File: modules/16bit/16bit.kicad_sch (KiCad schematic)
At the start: 56 parts, among them J1 Conn_01x08_Socket, J2 Conn_01x08_Socket, J5 USB_C_Receptacle_USB2.0_14P, SW1 K2-1808SN-A4SW-01, SW2 K2-1808SN-A4SW-01, SW3 K2-1808SN-A4SW-01, U1 RP2350_60QFN, U2 W25Q128JVS, U3 MCP6002-xSN, U4 PT8211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

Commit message: set 1k for the DAC low pass filter
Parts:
- R17, R18: value 10k -> 1k
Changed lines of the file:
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@@
 			)
 		)
-		(property "Value" "10k"
+		(property "Value" "1k"
 			(at 194.31 276.8599 0)
 			(effects
@@
 			)
 		)
-		(property "Value" "10k"
+		(property "Value" "1k"
 			(at 180.34 276.8599 0)
 			(effects

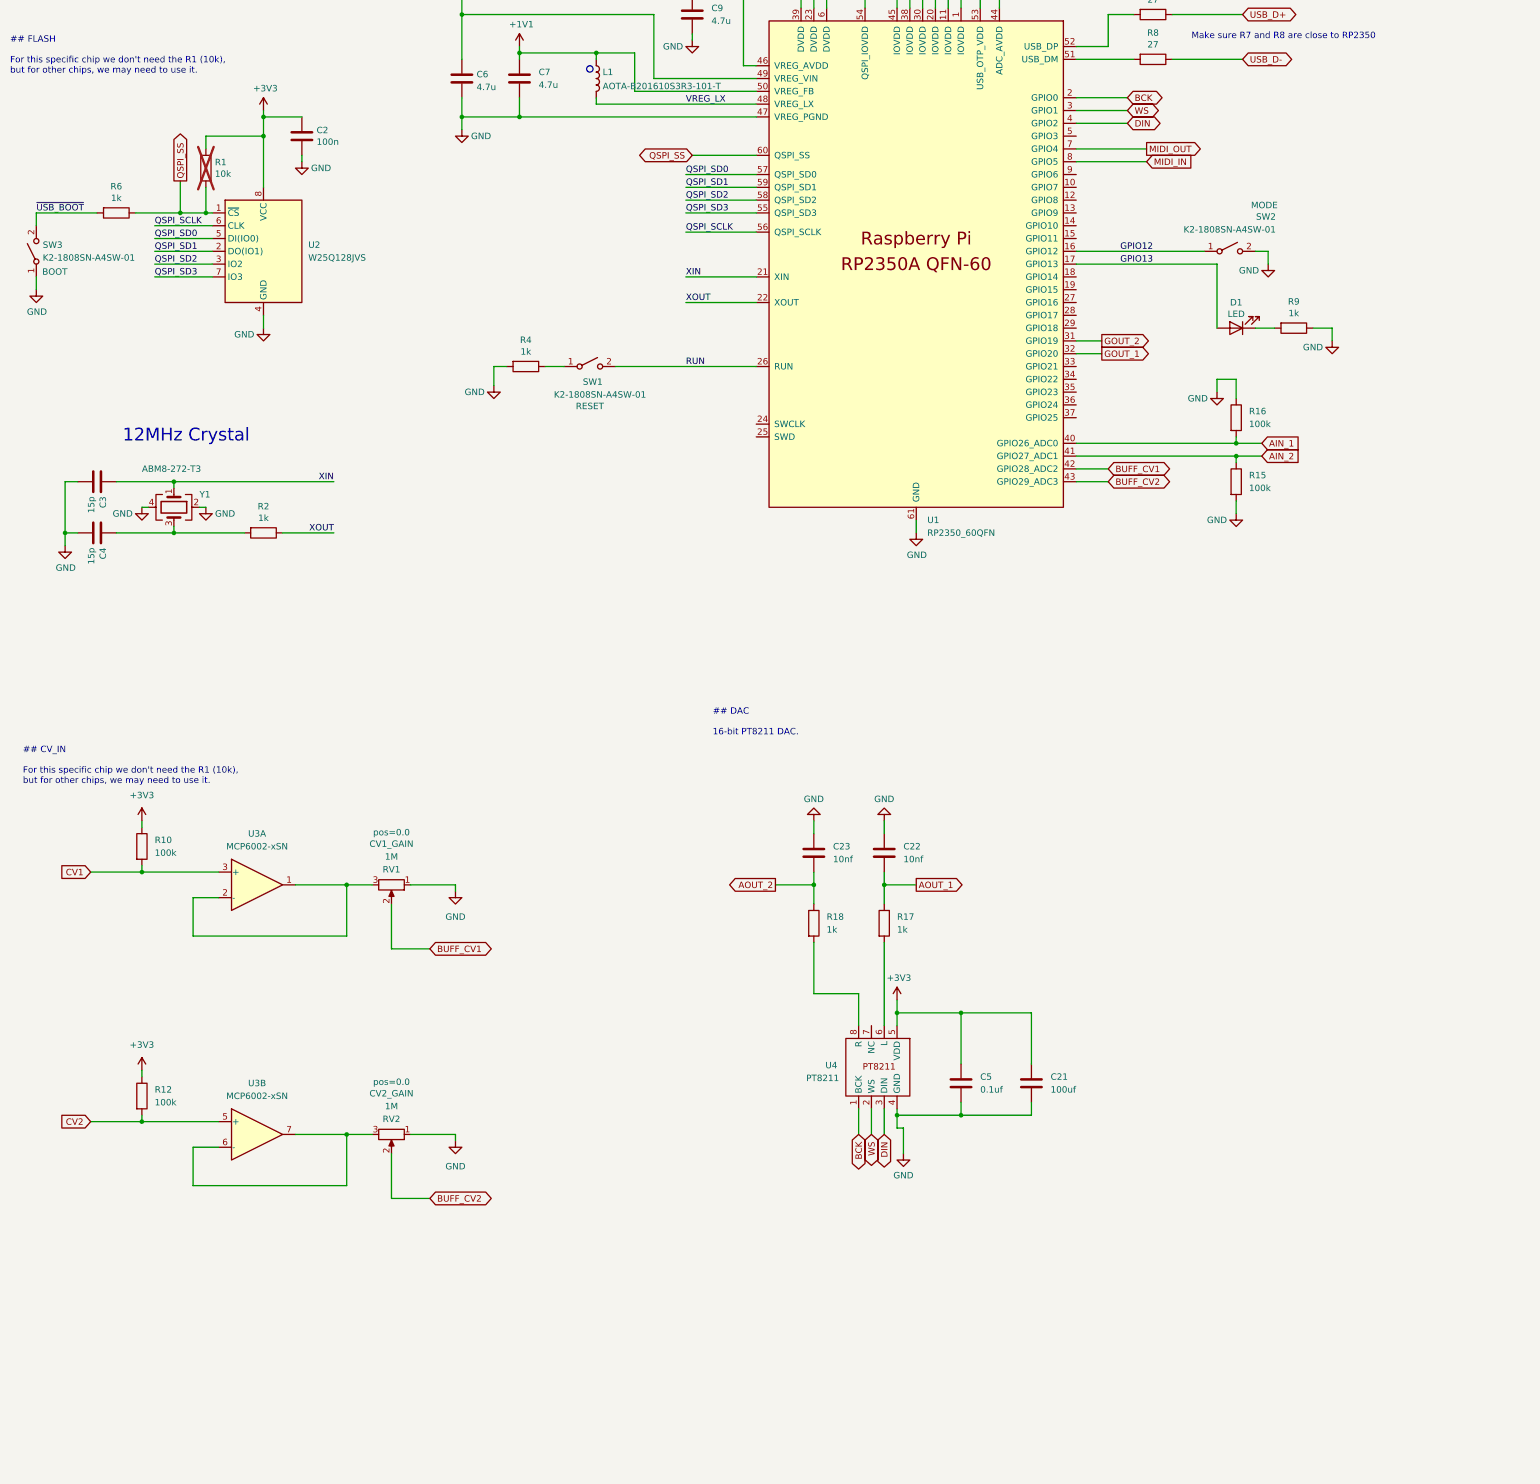
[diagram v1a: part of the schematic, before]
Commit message: Add 4677 PSRAM
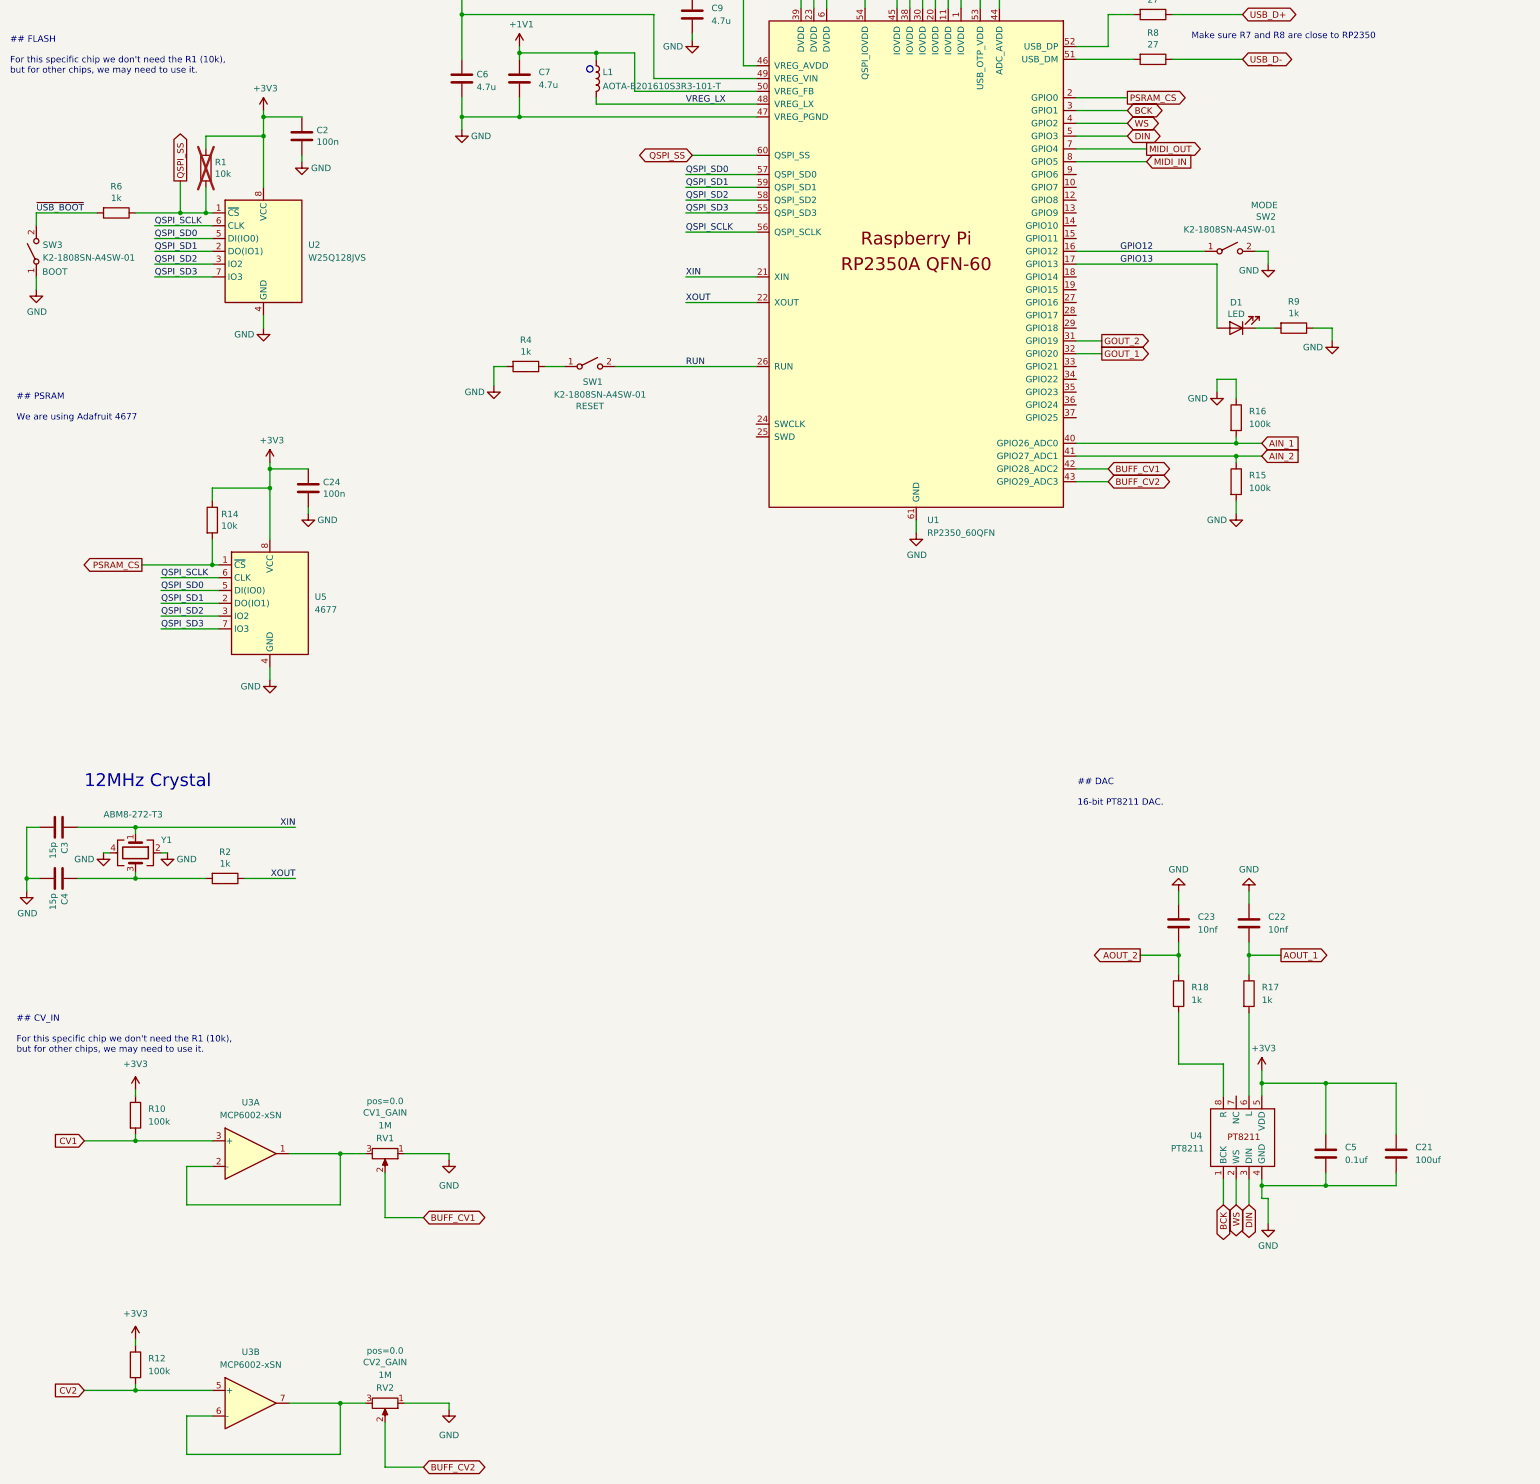
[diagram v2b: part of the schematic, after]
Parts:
- added C24: 100n, Capacitor_SMD:C_0402_1005Metric, symbol Device:C
- added R14: 10k, Resistor_SMD:R_0402_1005Metric, symbol Device:R
- added U5: 4677, BreadModular_MISC:SOIC-8 Generic, symbol Memory_Flash:W25Q128JVS
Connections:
- net +3V3: now also C24.1, R14.1, U5.8 (VCC)
- net BCK: now also U1.3 (GPIO1); no longer U1.2 (GPIO0)
- net DIN: now also U1.5 (GPIO3); no longer U1.4 (GPIO2)
- net GND: now also C24.2, U5.4 (GND)
- net QSPI_SCLK: now also U5.6 (CLK)
- net QSPI_SD0: now also U5.5 (DI(IO0))
- net QSPI_SD1: now also U5.2 (DO(IO1))
- net QSPI_SD2: now also U5.3 (IO2)
- net QSPI_SD3: now also U5.7 (IO3)
- net WS: now also U1.4 (GPIO2); no longer U1.3 (GPIO1)
- new net PSRAM_CS: R14.2, U1.2 (GPIO0), U5.1 (~{CS})
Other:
- note added: "## PSRAM We are using Adafruit 4677"
- moved on the sheet: C21, C22, C23, C3, C4, C5, R10, R12, R17, R18, R2, RV1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

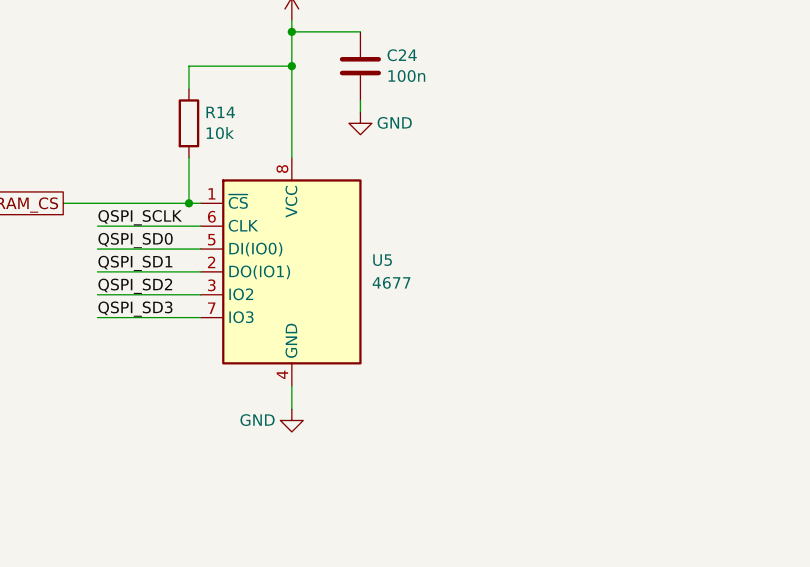
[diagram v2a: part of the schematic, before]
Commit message: 16bit: update PSRAM support
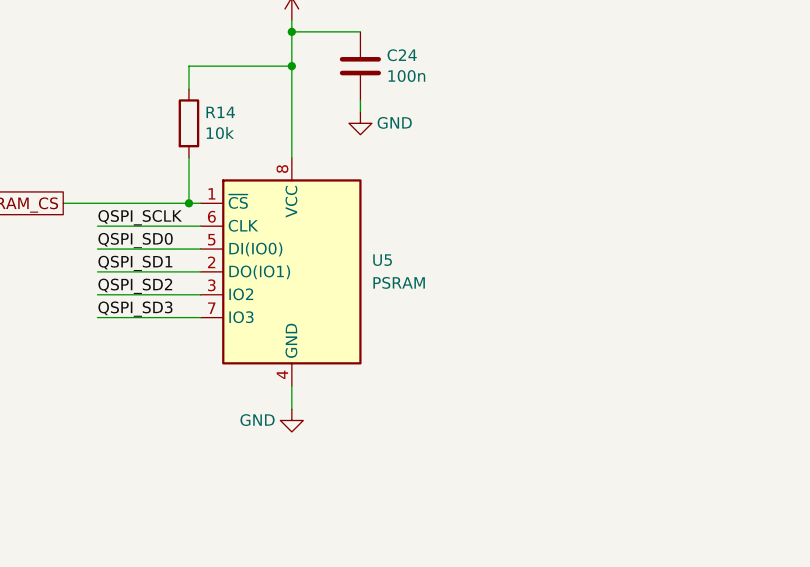
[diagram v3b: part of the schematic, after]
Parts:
- U5: value 4677 -> PSRAM
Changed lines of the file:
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@@
 			)
 		)
-		(property "Value" "4677"
+		(property "Value" "PSRAM"
 			(at 78.74 213.3599 0)
 			(effects

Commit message: 16bit: Add Ditial Audio In & Out support As of now this is currently hardware only. But this allows us to send audio out and in between 16bits digital using a single pin
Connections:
- net DGITIAL_AUDIO_IN: now reaches U1.12 (GPIO8)
- net DGITIAL_AUDIO_IN: now also J1.5 (Pin_5)
- net CV2: no longer names the net of R12.2, U3.5 (+)
- net CV2: no longer J1.5 (Pin_5)
- net GOUT_2 renamed DGITIAL_AUDIO_OUT
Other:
- moved on the sheet: J2
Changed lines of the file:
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@@
 	)
 	(junction
-		(at 43.18 368.3)
-		(diameter 0)
-		(color 0 0 0 0)
-	)
-	(junction
 		(at 214.63 81.28)
 		(diameter 0)
@@
 	(wire
 		(pts
+			(xy 240.03 132.08) (xy 229.87 132.08)
+		)
+		(stroke
+			(width 0)
+			(type default)
+		)
+	)
+	(wire
+		(pts
 			(xy 105.41 322.58) (xy 105.41 321.31)
 		)
@@
 	(wire
 		(pts
-			(xy 463.55 128.27) (xy 469.9 128.27)
+			(xy 83.82 370.84) (xy 83.82 381)
 		)
 		(stroke
@@
 	(wire
 		(pts
-			(xy 83.82 370.84) (xy 83.82 381)
+			(xy 229.87 114.3) (xy 240.03 114.3)
 		)
 		(stroke
@@
 	(wire
 		(pts
-			(xy 229.87 114.3) (xy 240.03 114.3)
+			(xy 266.7 307.34) (xy 279.4 307.34)
 		)
 		(stroke
@@
 	(wire
 		(pts
-			(xy 266.7 307.34) (xy 279.4 307.34)
+			(xy 21.59 266.7) (xy 21.59 269.24)
 		)
 		(stroke
@@
 	(wire
 		(pts
-			(xy 21.59 266.7) (xy 21.59 269.24)
+			(xy 537.21 71.12) (xy 539.75 71.12)
 		)
 		(stroke
@@
 	(wire
 		(pts
-			(xy 537.21 71.12) (xy 539.75 71.12)
+			(xy 40.64 69.85) (xy 40.64 80.01)
 		)
 		(stroke
@@
 	(wire
 		(pts
-			(xy 40.64 69.85) (xy 40.64 80.01)
+			(xy 199.39 93.98) (xy 199.39 81.28)
 		)
 		(stroke
@@
 	(wire
 		(pts
-			(xy 199.39 93.98) (xy 199.39 81.28)
+			(xy 469.9 128.27) (xy 463.55 128.27)
 		)
 		(stroke
@@
 	(wire
 		(pts
-			(xy 502.92 125.73) (xy 508 125.73)
-		)
-		(stroke
-			(width 0)
-			(type default)
-		)
-	)
-	(wire
-		(pts
 			(xy 201.93 93.98) (xy 201.93 81.28)
 		)
@@
 	(wire
 		(pts
-			(xy 502.92 120.65) (xy 508 120.65)
+			(xy 525.78 121.92) (xy 530.86 121.92)
 		)
 		(stroke
@@
 	(wire
 		(pts
-			(xy 33.02 368.3) (xy 43.18 368.3)
-		)
-		(stroke
-			(width 0)
-			(type default)
-		)
-	)
-	(wire
-		(pts
 			(xy 143.51 60.96) (xy 154.94 60.96)
 		)
@@
 	(wire
 		(pts
-			(xy 502.92 118.11) (xy 508 118.11)
+			(xy 525.78 119.38) (xy 530.86 119.38)
 		)
 		(stroke
@@
 	(wire
 		(pts
+			(xy 525.78 127) (xy 530.86 127)
+		)
+		(stroke
+			(width 0)
+			(type default)
+		)
+	)
+	(wire
+		(pts
 			(xy 537.21 212.09) (xy 529.59 212.09)
 		)
@@
 	(wire
 		(pts
-			(xy 502.92 115.57) (xy 508 115.57)
+			(xy 525.78 116.84) (xy 530.86 116.84)
 		)
 		(stroke
@@
 	(wire
 		(pts
-			(xy 502.92 123.19) (xy 508 123.19)
+			(xy 525.78 124.46) (xy 530.86 124.46)
 		)
 		(stroke
@@
 		)
 	)
-	(global_label "CV2"
-		(shape input)
-		(at 469.9 128.27 0)
-		(fields_autoplaced yes)
-		(effects
-			(font
-				(size 1.27 1.27)
-			)
-			(justify left)
-		)
-		(property "Intersheetrefs" "${INTERSHEET_REFS}"
-			(at 475.7991 128.27 0)
-			(effects
-				(font
-					(size 1.27 1.27)
-				)
-				(justify left)
-				(hide yes)
-			)
-		)
-	)
 	(global_label "GOUT_1"
 		(shape output)
@@
 	(global_label "GOUT_1"
 		(shape output)
-		(at 502.92 123.19 180)
+		(at 525.78 124.46 180)
 		(fields_autoplaced yes)
 		(effects
@@
 		)
 		(property "Intersheetrefs" "${INTERSHEET_REFS}"
-			(at 493.5133 123.19 0)
+			(at 516.3733 124.46 0)
 			(effects
 				(font
@@
 	(global_label "MIDI_OUT"
 		(shape output)
-		(at 502.92 115.57 180)
+		(at 525.78 116.84 180)
 		(fields_autoplaced yes)
 		(effects
@@
 		)
 		(property "Intersheetrefs" "${INTERSHEET_REFS}"
-			(at 492.0618 115.57 0)
+			(at 514.9218 116.84 0)
 			(effects
 				(font
@@
 		)
 	)
-	(global_label "GOUT_2"
+	(global_label "DGITIAL_AUDIO_OUT"
 		(shape output)
 		(at 234.95 160.02 0)
@@
 		)
 		(property "Intersheetrefs" "${INTERSHEET_REFS}"
-			(at 244.3567 160.02 0)
+			(at 255.3031 160.02 0)
 			(effects
 				(font
@@
 		)
 	)
-	(global_label "AIN_1"
+	(global_label "DGITIAL_AUDIO_IN"
 		(shape input)
-		(at 469.9 120.65 0)
+		(at 240.03 132.08 0)
 		(fields_autoplaced yes)
 		(effects
@@
 		)
 		(property "Intersheetrefs" "${INTERSHEET_REFS}"
-			(at 477.432 120.65 0)
+			(at 258.6898 132.08 0)
 			(effects
 				(font
@@
 		)
 	)
-	(global_label "CV2"
+	(global_label "DGITIAL_AUDIO_IN"
 		(shape input)
-		(at 33.02 368.3 180)
+		(at 469.9 128.27 0)
 		(fields_autoplaced yes)
 		(effects
@@
 				(size 1.27 1.27)
 			)
-			(justify right)
+			(justify left)
 		)
 		(property "Intersheetrefs" "${INTERSHEET_REFS}"
-			(at 26.4667 368.3 0)
+			(at 488.5598 128.27 0)
 			(effects
 				(font
 					(size 1.27 1.27)
 				)
-				(justify right)
+				(justify left)
+				(hide yes)
+			)
+		)
+	)
+	(global_label "AIN_1"
+		(shape input)
+		(at 469.9 120.65 0)
+		(fields_autoplaced yes)
+		(effects
+			(font
+				(size 1.27 1.27)
+			)
+			(justify left)
+		)
+		(property "Intersheetrefs" "${INTERSHEET_REFS}"
+			(at 477.432 120.65 0)
+			(effects
+				(font
+					(size 1.27 1.27)
+				)
+				(justify left)
 				(hide yes)
 			)
@@
 	(global_label "AOUT_1"
 		(shape output)
-		(at 502.92 118.11 180)
+		(at 525.78 119.38 180)
 		(fields_autoplaced yes)
 		(effects
@@
 		)
 		(property "Intersheetrefs" "${INTERSHEET_REFS}"
-			(at 493.6947 118.11 0)
+			(at 516.5547 119.38 0)
 			(effects
 				(font
@@
 		)
 	)
-	(global_label "GOUT_2"
-		(shape output)
-		(at 502.92 125.73 180)
-		(fields_autoplaced yes)
-		(effects
-			(font
-				(size 1.27 1.27)
-			)
-			(justify right)
-		)
-		(property "Intersheetrefs" "${INTERSHEET_REFS}"
-			(at 493.5133 125.73 0)
-			(effects
-				(font
-					(size 1.27 1.27)
-				)
-				(justify right)
-				(hide yes)
-			)
-		)
-	)
 	(global_label "USB_D-"
 		(shape bidirectional)
@@
 	(global_label "AOUT_2"
 		(shape output)
-		(at 502.92 120.65 180)
+		(at 525.78 121.92 180)
 		(fields_autoplaced yes)
 		(effects
@@
 		)
 		(property "Intersheetrefs" "${INTERSHEET_REFS}"
-			(at 493.6947 120.65 0)
+			(at 516.5547 121.92 0)
 			(effects
 				(font
@@
 		)
 	)
+	(global_label "DGITIAL_AUDIO_OUT"
+		(shape output)
+		(at 525.78 127 180)
+		(fields_autoplaced yes)
+		(effects
+			(font
+				(size 1.27 1.27)
+			)
+			(justify right)
+		)
+		(property "Intersheetrefs" "${INTERSHEET_REFS}"
+			(at 505.4269 127 0)
+			(effects
+				(font
+					(size 1.27 1.27)
+				)
+				(justify right)
+				(hide yes)
+			)
+		)
+	)
 	(symbol
 		(lib_id "power:+3V3")
@@
 	(symbol
 		(lib_id "Connector:Conn_01x05_Socket")
-		(at 513.08 120.65 0)
+		(at 535.94 121.92 0)
 		(unit 1)
 		(exclude_from_sim no)
@@
 		(dnp no)
 		(property "Reference" "J2"
-			(at 514.35 119.634 90)
+			(at 537.21 120.904 90)
 			(effects
 				(font
@@
 		)
 		(property "Value" "Conn_01x08_Socket"
-			(at 516.382 120.142 90)
+			(at 539.242 121.412 90)
 			(effects
 				(font
@@
 		)
 		(property "Footprint" "Connector_PinSocket_2.54mm:PinSocket_1x05_P2.54mm_Vertical"
-			(at 513.08 120.65 0)
+			(at 535.94 121.92 0)
 			(effects
 				(font
@@
 		)
 		(property "Datasheet" "~"
-			(at 513.08 120.65 0)
+			(at 535.94 121.92 0)
 			(effects
 				(font
@@
 		)
 		(property "Description" "Generic connector, single row, 01x05, script generated"
-			(at 513.08 120.65 0)
+			(at 535.94 121.92 0)
 			(effects
 				(font
